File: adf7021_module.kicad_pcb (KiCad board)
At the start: 4 copper layers, 52 x 26 mm, 68 parts, among them J1 Conn_02x10_Counter_Clockwise, J2 Conn_Coaxial, J3 Conn_Coaxial, J4 Conn_02x10_Counter_Clockwise, U1 ADF7021, X1 19.68MHz

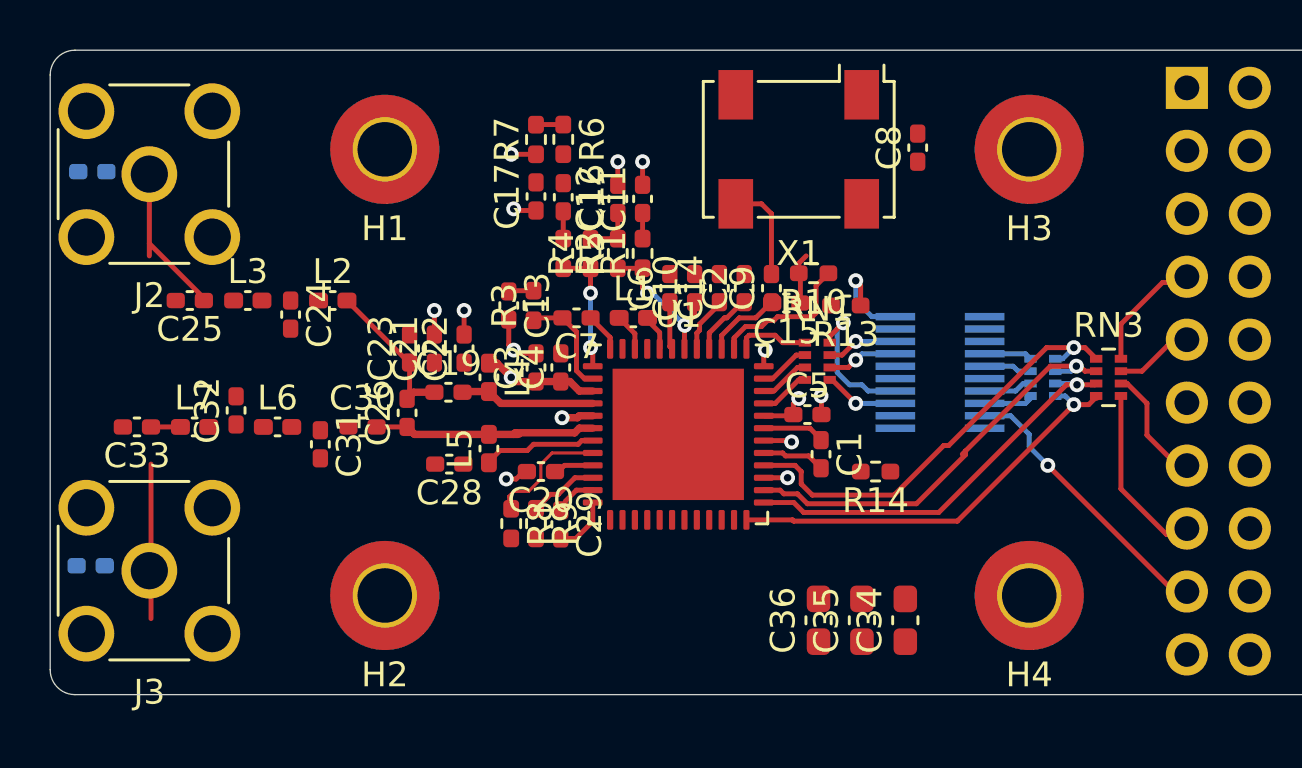
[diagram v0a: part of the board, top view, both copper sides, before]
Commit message: Adding mechanical dimensions, adjusting location of J1
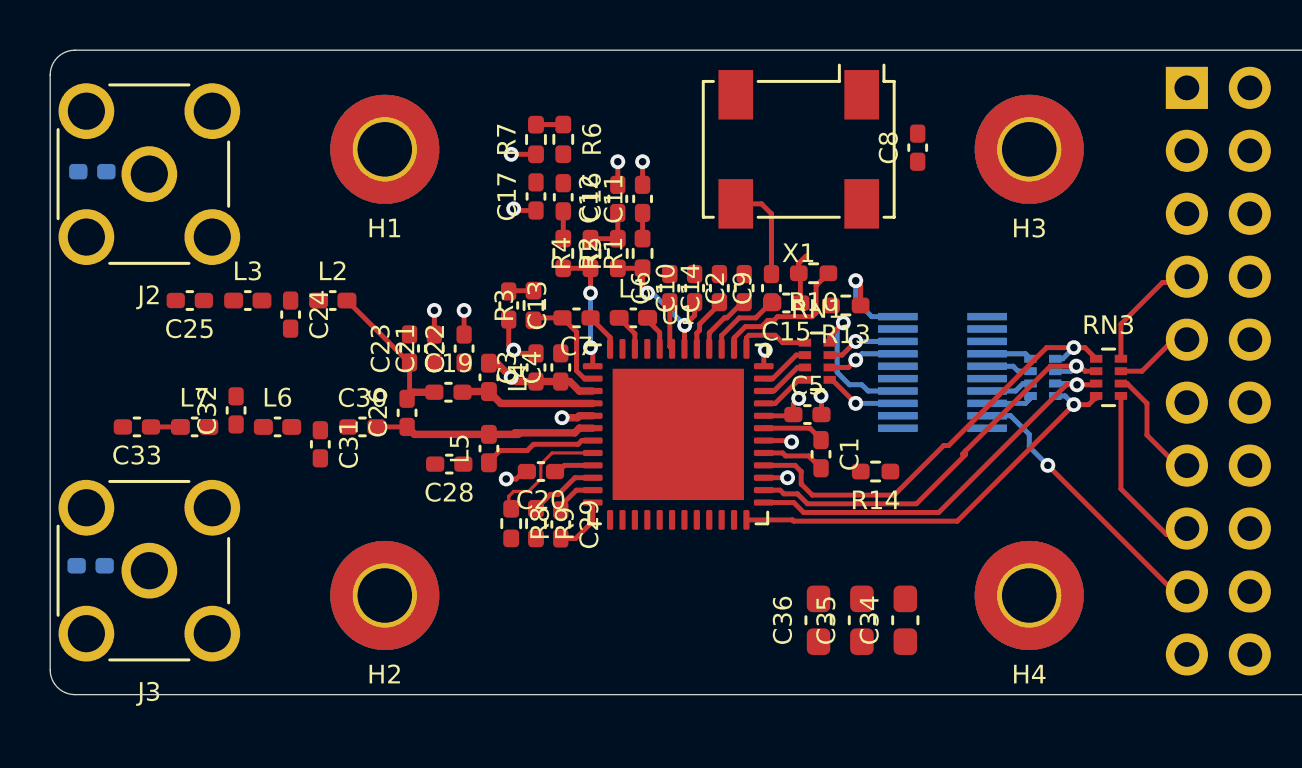
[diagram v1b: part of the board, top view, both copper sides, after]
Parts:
- moved J1 0.10 mm to (142.0, 57.5)
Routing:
- net Net-(C18-Pad1): track 6.51 -> 0.00 mm
- net Net-(C27-Pad2): track 7.41 -> 1.18 mm

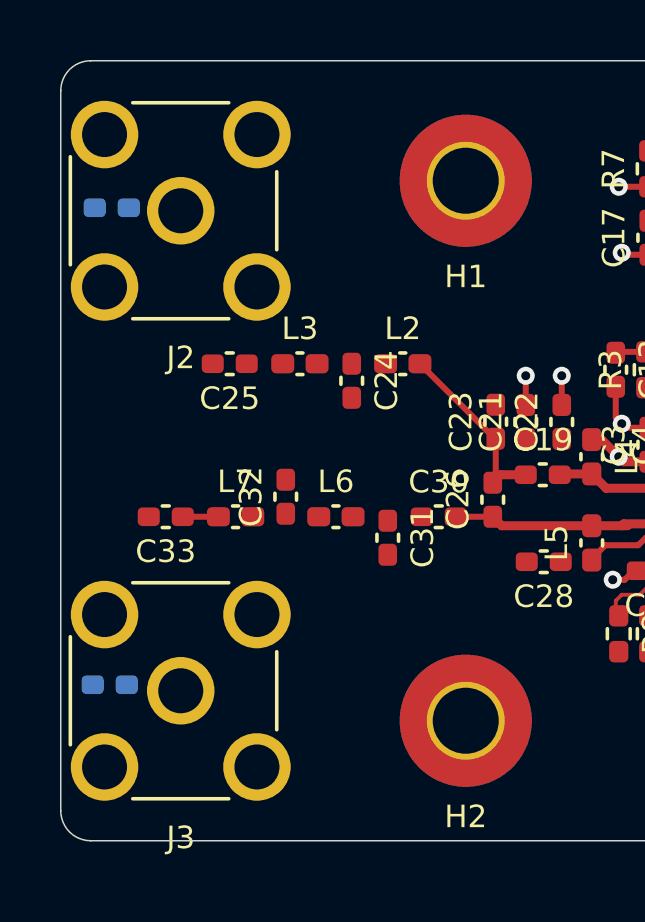
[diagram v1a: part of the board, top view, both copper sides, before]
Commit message: Giving SMA's more generous spacing from edge
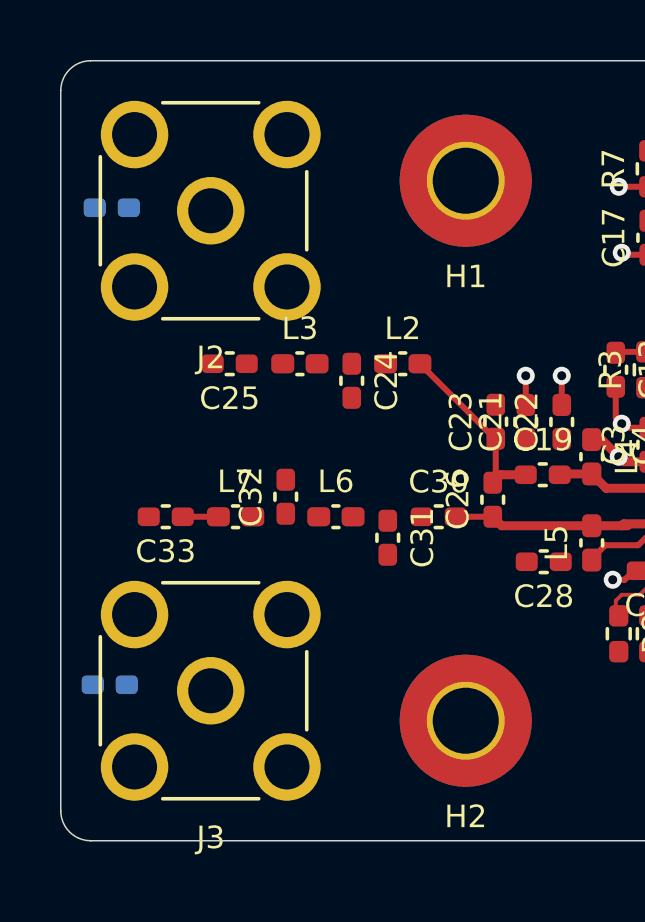
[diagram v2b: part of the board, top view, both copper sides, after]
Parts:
- moved J2 1.00 mm to (111.0, 49.5)
- moved J3 1.00 mm to (111.0, 65.5)
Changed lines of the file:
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@@
   )
   (module Connector_Coaxial:SMA_Molex_73251-2200_Horizontal (layer F.Cu)
-    (at 110 65.5 90)
+    (at 111 65.5 90)
     (descr https://www.molex.com/webdocs/datasheets/pdf/en-us/0732512200_RF_COAX_CONNECTORS.pdf)
     (tags "SMA THT Female Jack Horizontal")
@@
   )
   (module Connector_Coaxial:SMA_Molex_73251-2200_Horizontal (layer F.Cu)
-    (at 110 49.5 90)
+    (at 111 49.5 90)
     (descr https://www.molex.com/webdocs/datasheets/pdf/en-us/0732512200_RF_COAX_CONNECTORS.pdf)
     (tags "SMA THT Female Jack Horizontal")

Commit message: Adding 3V3/GND planes to internal layers
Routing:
- added copper zone on In2.Cu, net +3V3
- added copper zone on In1.Cu, net GND
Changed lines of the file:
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@@
   (segment (start 151.09 56.41) (end 151.71 56.41) (width 0.2) (layer F.Cu) (net 57))
   (segment (start 150.05 57.45) (end 151.09 56.41) (width 0.2) (layer F.Cu) (net 57))
+  (zone (net 1) (net_name GND) (layer In1.Cu) (hatch edge 0.508)
+    (connect_pads (clearance 0.508))
+    (min_thickness 0.254)
+    (fill yes (arc_segments 32) (thermal_gap 0.508) (thermal_bridge_width 0.508))
+    (polygon
+      (pts
+        (xy 165 75) (xy 100 75) (xy 100 40) (xy 165 40)
+      )
+    )
+  )
+  (zone (net 3) (net_name +3V3) (layer In2.Cu) (hatch edge 0.508)
+    (connect_pads (clearance 0.508))
+    (min_thickness 0.254)
+    (fill yes (arc_segments 32) (thermal_gap 0.508) (thermal_bridge_width 0.508))
+    (polygon
+      (pts
+        (xy 165 75) (xy 100 75) (xy 100 40) (xy 165 40)
+      )
+    )
+  )
 )

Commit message: Shrinking vias to OSH Park spec (10 mil drill, 20 mil dia)
This is larger than JLCPCB's spec. Additionally, while OSH Park can
technically handle 18 mil dia, that results in 4 mil annular rings,
which may push the PCB tech a little too far. (Minimum trace/space is
5 mil.)
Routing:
- net CE: track 17.2 -> 18.4 mm
- net SLE: track 16.6 -> 17.7 mm
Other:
- net class Default: via_dia 0.6 -> 0.508; via_drill 0.3 -> 0.254
- rule via_min_drill: 0.3 -> 0.254
- rule via_min_size: 0.4 -> 0.508

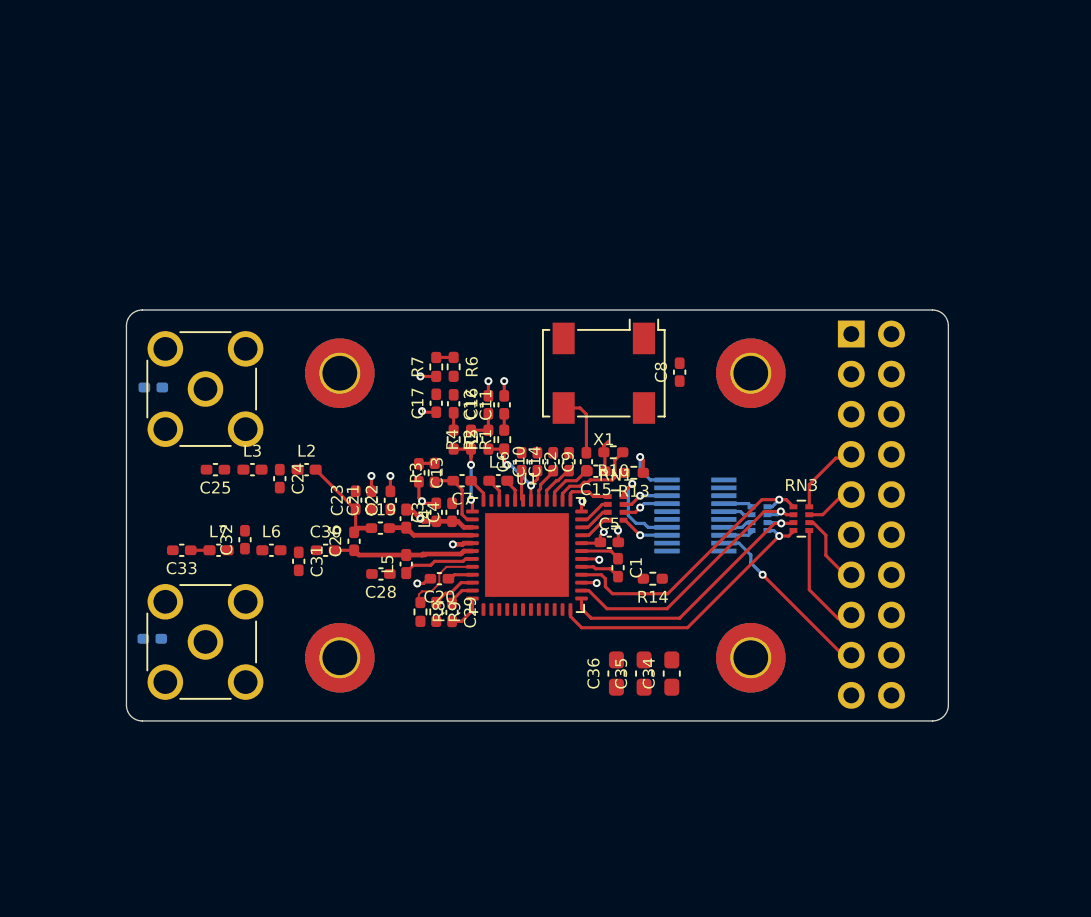
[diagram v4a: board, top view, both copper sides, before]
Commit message: Routing WIP
 * Trying for symmetrical filter layout
 * Moving non-essential circuitry (ie: FM_MOD filter) away from U1
 * GND pad for J1 on bottom
 * Trying to have SMD orientation match schematic (ie: L5/C28)
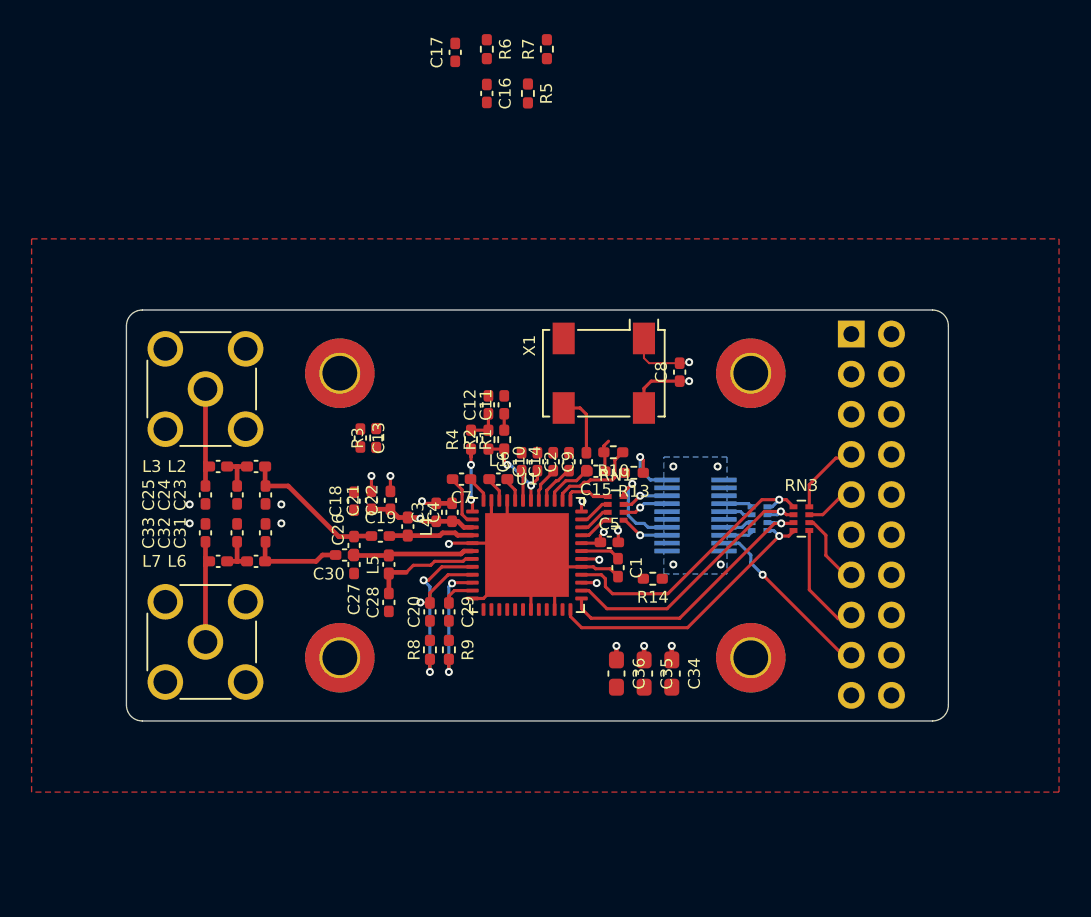
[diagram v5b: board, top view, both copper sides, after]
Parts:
- C18, C27: moved to F.Cu
- moved R5 22.4 mm to (131.4, 30.8)
- moved C17 22.2 mm to (126.8, 28.2)
- moved R7 21.3 mm to (132.6, 28.0)
- moved R6 20.2 mm to (128.8, 28.0)
- moved C16 19.7 mm to (128.8, 30.8)
- moved C18 14.6 mm to (120.4, 56.6), turned to 90 degrees
- moved C27 13.6 mm to (120.4, 60.6), turned to 270 degrees
- moved C23 5.71 mm to (114.8, 56.2), turned to 270 degrees
- moved C13 4.30 mm to (120.8, 52.6)
- moved R3 4.30 mm to (121.8, 52.6)
- moved L2 3.21 mm to (114.2, 54.4)
- moved C24 2.89 mm to (113.0, 56.2)
- moved C31 2.77 mm to (114.8, 58.6), turned to 90 degrees
- moved R9 2.53 mm to (126.4, 66.0), turned to 90 degrees
- moved R8 2.47 mm to (125.2, 66.0), turned to 90 degrees
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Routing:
- net GND: track 15.8 -> 41.2 mm, vias 10 -> 14
- net +3V3: track 13.0 -> 24.7 mm, vias 2 -> 7
- net Net-(C18-Pad1): track 0.00 -> 6.32 mm
- net Net-(C30-Pad1): track 0.00 -> 5.87 mm
- net Net-(C27-Pad2): track 1.18 -> 6.62 mm
- net /R_LNA: track 4.97 -> 10.2 mm, vias 0 -> 2
- net /RSET: track 2.81 -> 7.80 mm, vias 0 -> 2
- net Net-(C19-Pad1): track 6.28 -> 9.28 mm
- net Net-(C32-Pad1): track 0.00 -> 2.49 mm
- net Net-(C24-Pad1): track 0.00 -> 2.49 mm
- net Net-(C28-Pad1): track 4.59 -> 6.93 mm
- net /RFIN: track 9.35 -> 7.60 mm
- net /CREG1: track 4.36 -> 3.16 mm
- net Net-(C16-Pad2): track 1.10 -> 0.00 mm
- net FM_MOD: track 12.5 -> 11.4 mm
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- added copper zone on B.Cu, net GND
- added copper zone on F.Cu, net GND

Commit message: Most traces routed, except debug U.FL's
 * Care to prevent plane slots on In1/In2 w/ vias
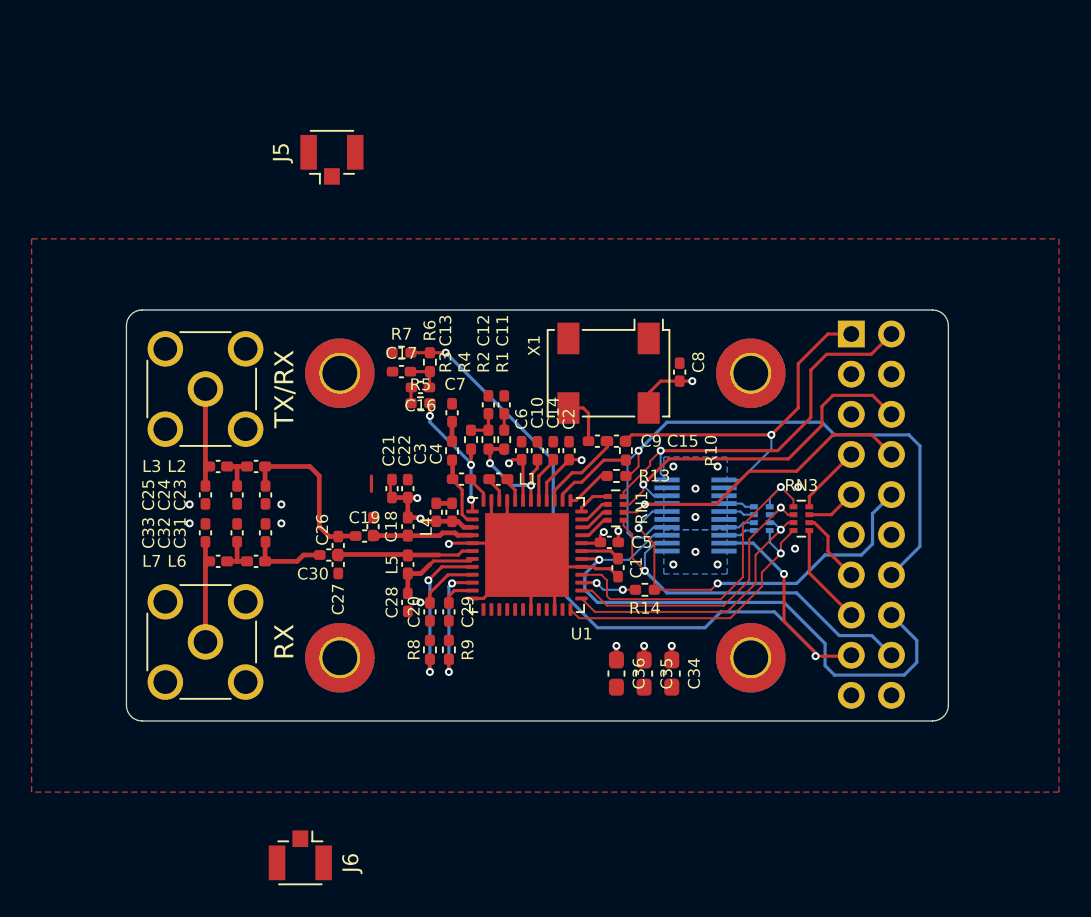
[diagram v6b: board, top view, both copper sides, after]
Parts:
- added J5: Conn_Coaxial, Connector_Coaxial:U.FL_Hirose_U.FL-R-SMT-1_Vertical, F.Cu at (119.0, 35.0)
- added J6: Conn_Coaxial, Connector_Coaxial:U.FL_Hirose_U.FL-R-SMT-1_Vertical, F.Cu at (117.0, 79.0)
- R13: value 1k -> 22
- moved R7 21.3 mm to (123.4, 47.2), turned to 0 degrees
- moved R5 20.7 mm to (124.6, 50.4), turned to 0 degrees
- moved C17 20.5 mm to (123.4, 48.4), turned to 0 degrees
- moved R6 20.1 mm to (125.2, 47.8)
- moved C16 19.1 mm to (124.6, 49.4), turned to 180 degrees
- moved C13 6.02 mm to (126.6, 51.0), turned to 90 degrees
- moved R3 4.87 mm to (126.6, 53.4)
- moved C15 2.30 mm to (137.0, 52.8)
- moved C18 2.00 mm to (121.6, 58.2), turned to 270 degrees
- moved C21 1.50 mm to (122.8, 55.8)
- moved C9 1.48 mm to (135.8, 52.8), turned to 180 degrees
- moved C22 1.33 mm to (123.8, 55.8)
- moved C28 1.20 mm to (123.8, 63.0)
- moved L5 1.20 mm to (123.8, 60.6)
- moved R13 1.12 mm to (137.0, 55.0)
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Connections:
- C25 pad 1: Net-(C18-Pad1) -> Net-(C25-Pad1)
- C33 pad 1: Net-(C27-Pad2) -> Net-(C33-Pad1)
- J1 pad 18: SWD -> ADCIN
- J1 pad 19: ADCIN -> SWD
- J2 pad 1: Net-(C18-Pad1) -> Net-(C25-Pad1)
- J3 pad 1: Net-(C27-Pad2) -> Net-(C33-Pad1)
- J4 pad 16: SWD -> ADCIN
- J4 pad 18: ADCIN -> SWD
- L3 pad 1: Net-(C18-Pad1) -> Net-(C25-Pad1)
- L7 pad 1: Net-(C27-Pad2) -> Net-(C33-Pad1)
- R13 pad 1: CLKOUT -> MUXOUT
- RN1 pad 8: MUXOUT -> CLKOUT
- U1 pad 36: Net-(R13-Pad2) -> Net-(RN1-Pad1)
- U1 pad 37: Net-(RN1-Pad1) -> Net-(R13-Pad2)
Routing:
- net FM_MOD: track 11.4 -> 52.0 mm, vias 1 -> 3
- net ADCIN: track 1.15 -> 36.5 mm
- net MUXOUT: track 5.79 -> 38.5 mm
- net SREAD: track 0.00 -> 25.3 mm, vias 0 -> 2
- net CLKOUT: track 3.75 -> 25.3 mm
- net CLK_IN: track 2.05 -> 23.5 mm, vias 0 -> 1
- net SWD: track 3.04 -> 24.3 mm
- net TxRxCLK: track 2.88 -> 23.1 mm
- net TxRxData: track 2.88 -> 20.9 mm
- net Net-(C33-Pad1): track 0.00 -> 6.62 mm
- net Net-(C27-Pad2): track 6.62 -> 0.00 mm
- net Net-(C25-Pad1): track 0.00 -> 6.32 mm
- net Net-(C18-Pad1): track 6.32 -> 0.00 mm
- net GND: track 41.2 -> 35.9 mm, vias 14 -> 12
- net /VCOIN: track 4.49 -> 9.47 mm, vias 2 -> 3
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- added copper zone on B.Cu, net +3V3
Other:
- board text added: "RX"
- board text added: "TX/RX"
